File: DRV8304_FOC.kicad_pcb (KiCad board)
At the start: 4 copper layers, 49.5 x 30.2 mm, 63 parts, among them J2 Conn_01x03, J3 Conn_01x03, Q1 SIRA18ADP, Q2 SIRA18ADP, Q3 SIRA18ADP, Q4 SIRA18ADP, Q5 SIRA18ADP, Q6 SIRA18ADP, SW2 SW_Push, U1 TPS565208, U2 TPS259850RQPR, U3 DRV8304HRHAR, U4 STM32F412CEUx, U5 AS5055A, Y1 Crystal_GND23

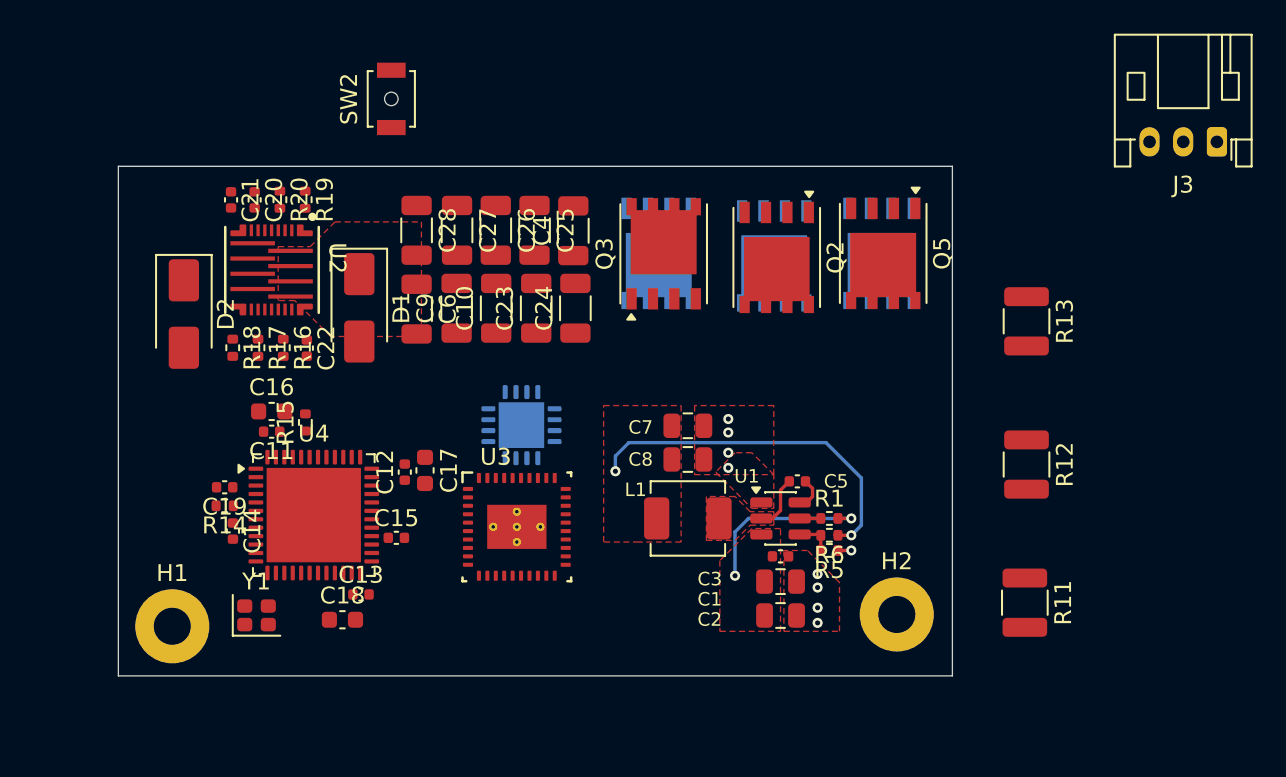
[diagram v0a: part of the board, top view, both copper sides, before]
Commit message: Modified encoder sch, modified layout
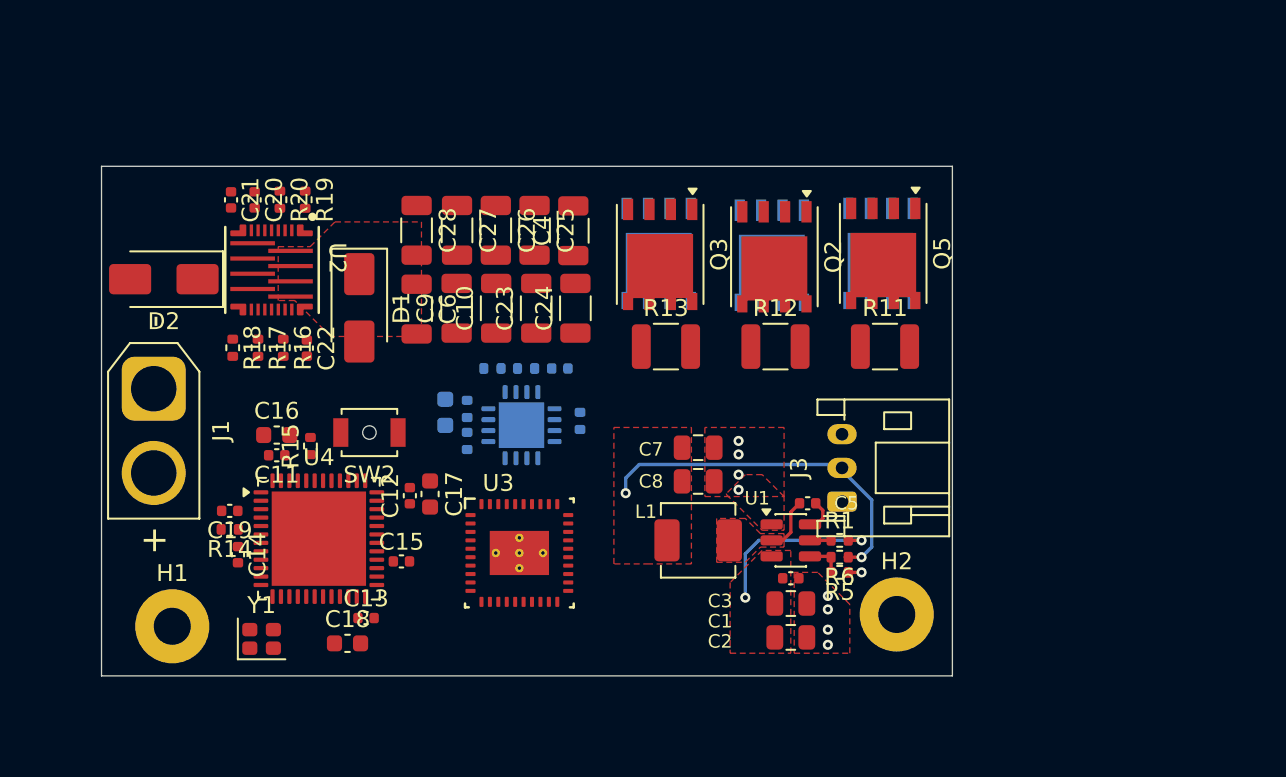
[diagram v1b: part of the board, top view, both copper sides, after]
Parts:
- added C29: 4.7uF, Capacitor_SMD:C_0603_1608Metric, B.Cu at (91.9, 70.4)
- added C30: 100nF, Capacitor_SMD:C_0402_1005Metric, B.Cu at (98.7, 67.8)
- added J1: Conn_01x02, Connector_AMASS:AMASS_XT30U-M_1x02_P5.0mm_Vertical, F.Cu at (74.6, 69.0)
- added R10: 22R, Resistor_SMD:R_0402_1005Metric, B.Cu at (93.2, 72.1)
- added R21: 10k, Resistor_SMD:R_0402_1005Metric, B.Cu at (96.7, 67.8)
- added R22: 22R, Resistor_SMD:R_0402_1005Metric, B.Cu at (99.9, 70.9)
- added R7: 15R, Resistor_SMD:R_0402_1005Metric, B.Cu at (93.2, 70.2)
- added R9: 22R, Resistor_SMD:R_0402_1005Metric, B.Cu at (94.7, 67.8)
- moved J3 30.8 mm to (115.5, 75.7), turned to 90 degrees
- moved R13 21.5 mm to (105.0, 66.5), turned to 0 degrees
- moved SW2 19.8 mm to (87.4, 71.6), turned to 180 degrees
- moved R11 17.3 mm to (118.0, 66.5), turned to 0 degrees
- moved R12 16.5 mm to (111.5, 66.5), turned to 0 degrees
- moved D2 2.39 mm to (75.2, 62.5), turned to 180 degrees
- moved U3 1.56 mm to (96.3, 78.7)
- moved C1 1.44 mm to (112.4, 81.7)
- moved C3 1.44 mm to (112.4, 80.2)
- moved C7 1.44 mm to (106.9, 72.5)
- moved C8 1.44 mm to (106.9, 74.5)
- moved L1 1.44 mm to (106.9, 78.0)
- moved R1 1.44 mm to (115.3, 78.0)
- moved R6 1.44 mm to (115.3, 79.0)
- moved U1 1.44 mm to (112.4, 78.0)
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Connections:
- U5 pad 1: unconnected-(U5-MOSI-Pad1) -> Net-(U5-MOSI)
- U5 pad 10: unconnected-(U5-~{EN_INT}-Pad10) -> GND
- U5 pad 11: unconnected-(U5-VDDp-Pad11) -> 3V3
- U5 pad 12: unconnected-(U5-VDD-Pad12) -> Net-(U5-VDD)
- U5 pad 13: unconnected-(U5-VSS-Pad13) -> GND
- U5 pad 14: unconnected-(U5-WM-Pad14) -> 3V3
- U5 pad 15: unconnected-(U5-~{INT}-Pad15) -> ~{INT}
- U5 pad 2: unconnected-(U5-MISO-Pad2) -> Net-(U5-MISO)
- U5 pad 3: unconnected-(U5-SCK-Pad3) -> Net-(U5-SCK)
- U5 pad 4: unconnected-(U5-~{SS}-Pad4) -> ~{SS}
- U5 pad 9: unconnected-(U5-TEST-Pad9) -> GND
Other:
- board size 49.5 x 30.2 mm -> 50.5 x 30.2 mm

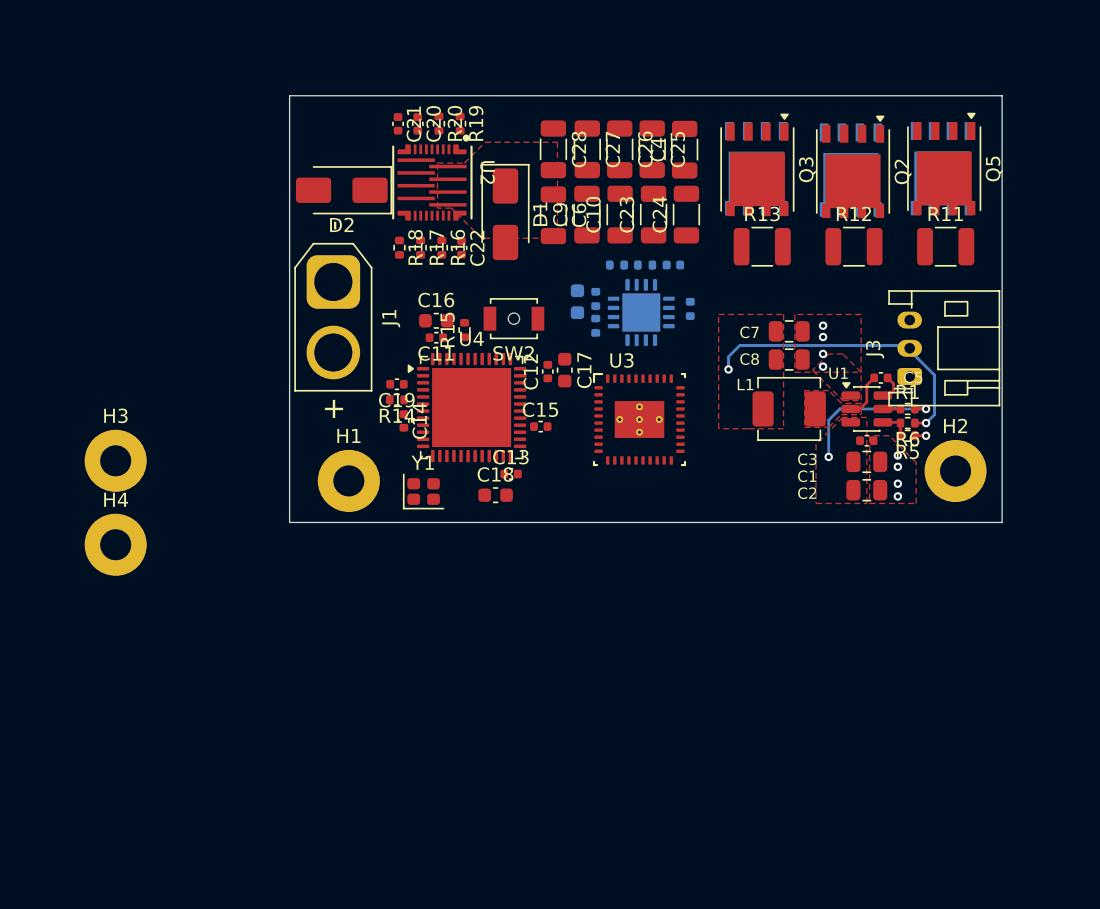
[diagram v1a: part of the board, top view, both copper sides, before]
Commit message: Replace buck converter with LDO
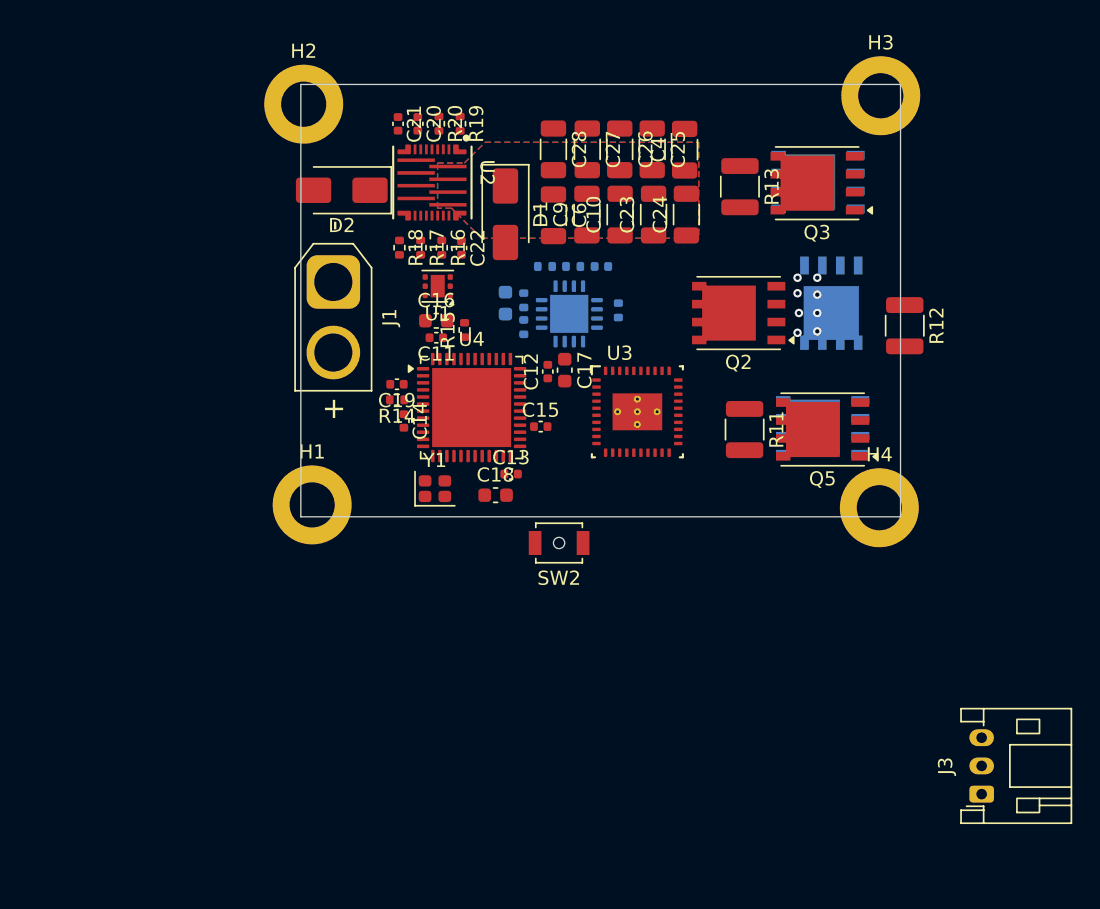
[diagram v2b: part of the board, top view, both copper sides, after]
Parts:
- removed C1, C2: 22uF, Capacitor_SMD:C_0805_2012Metric
- removed C3, C5: 0.1uF, Capacitor_SMD:C_0402_1005Metric
- removed C7, C8: 22u, Capacitor_SMD:C_0805_2012Metric
- removed L1: 3.3u, Inductor_SMD:L_APV_APH0420
- removed R1: 0, Resistor_SMD:R_0402_1005Metric
- removed R5: 10k, Resistor_SMD:R_0402_1005Metric
- removed R6: 13.7k, Resistor_SMD:R_0402_1005Metric
- H1, H2, H3, H4: footprint MountingHole:MountingHole_2.2mm_M2_Pad -> MountingHole:MountingHole_3.2mm_M3_DIN965_Pad
- U1: value TPS565208 -> TPS7A2633DRVR; footprint Package_TO_SOT_SMD:SOT-23-6 -> Package_SON:WSON-6-1EP_2x2mm_P0.65mm_EP1x1.6mm
- moved H3 60.1 mm to (113.4, 55.8)
- moved H4 54.2 mm to (113.3, 85.0)
- moved H2 53.0 mm to (72.5, 56.4)
- moved U1 31.6 mm to (82.0, 69.3), turned to 180 degrees
- moved J3 30.0 mm to (120.6, 105.3)
- moved Q5 20.4 mm to (109.3, 79.4), turned to 180 degrees
- moved Q6 20.2 mm to (109.3, 79.3), turned to 180 degrees
- moved R11 19.3 mm to (103.8, 79.4), turned to -90 degrees
- moved SW2 16.2 mm to (90.6, 87.5)
- moved Q2 12.9 mm to (103.3, 71.2), turned to 180 degrees
- moved Q1 9.53 mm to (109.9, 70.5)
- moved R12 6.66 mm to (115.1, 72.1), turned to -90 degrees
- moved C30 5.10 mm to (93.6, 67.9)
- moved R10 5.10 mm to (88.1, 72.2)
- moved R21 5.10 mm to (91.6, 67.9)
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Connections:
- U1 pad 1: GND -> unconnected-(U1-OUT-Pad1)
- U1 pad 2: Net-(U1-SW) -> unconnected-(U1-NC-Pad2)
- U1 pad 3: Vm -> unconnected-(U1-PG-Pad3)
- U1 pad 4: Net-(U1-VFB) -> unconnected-(U1-EN-Pad4)
- U1 pad 5: Net-(U1-EN) -> EPAD
- U1 pad 6: Net-(U1-VBST) -> unconnected-(U1-IN-Pad6)
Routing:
- net 3V3: track 21.3 -> 0.00 mm, vias 2 -> 0
- net Vm: track 10.8 -> 0.00 mm
- net Net-(U1-SW): track 3.27 -> 0.00 mm
- net Net-(U1-VFB): track 2.48 -> 0.00 mm
- net Net-(U1-VBST): track 2.38 -> 0.00 mm
- net Net-(U1-EN): track 1.44 -> 0.00 mm
- net GND: track 0.98 -> 0.00 mm, vias 9 -> 0
- net unconnected-(Q2-G-Pad2): vias 0 -> 4
- net unconnected-(Q1-G-Pad2): vias 0 -> 1
- net Vin: vias 2 -> 1
- net Net-(Q1-S): vias 0 -> 1
- net (no net): vias 0 -> 1
- added copper zone on B.Cu, net Vin
- added copper zone on In1.Cu, net Vin
- added copper zone on In2.Cu, net Vin
- removed copper zone on F.Cu, net 3V3
- removed copper zone on F.Cu, net GND
- removed copper zone on F.Cu, net Net-(U1-SW)
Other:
- board size 50.5 x 30.2 mm -> 42.5 x 30.6 mm

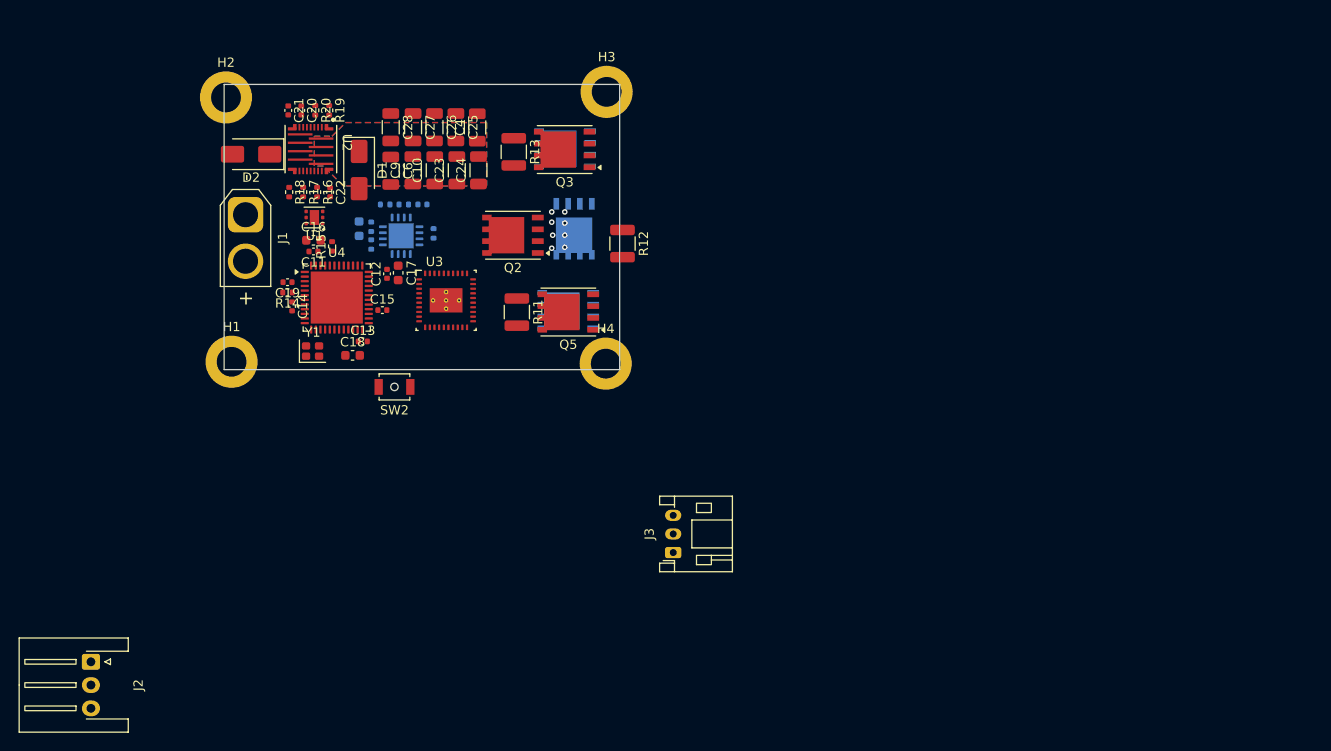
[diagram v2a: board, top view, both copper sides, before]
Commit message: Add buck back, changed board shape, replace cer cap with alu cap
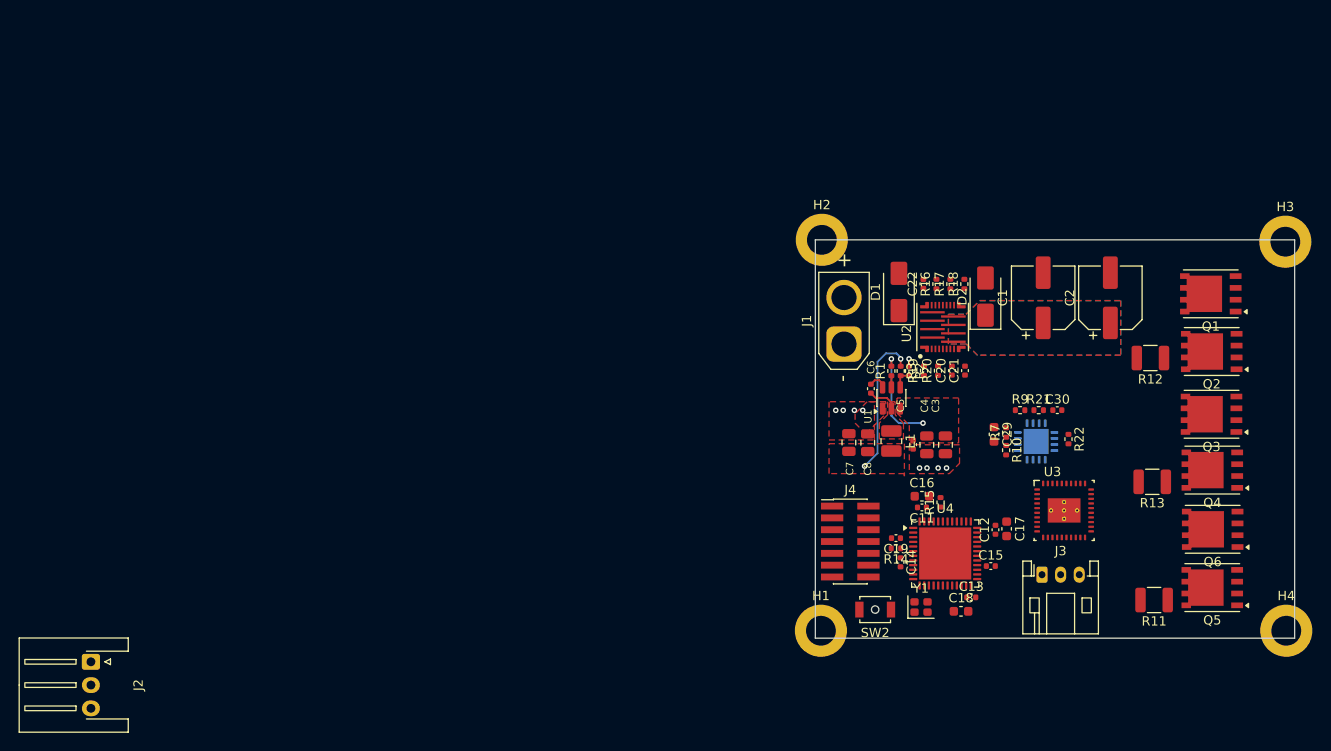
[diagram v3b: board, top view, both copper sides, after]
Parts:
- removed C10, C23, C24, C25, C26, C27, C28, C9: 22uF, Capacitor_SMD:C_1206_3216Metric
- added C1: C_Polarized, Capacitor_SMD:CP_Elec_6.3x7.7, F.Cu at (160.3, 77.9)
- added C2: C_Polarized, Capacitor_SMD:CP_Elec_6.3x7.7, F.Cu at (167.5, 77.9)
- added C3: 22u, Capacitor_SMD:C_0805_2012Metric, F.Cu at (149.8, 93.7)
- added C5: 0.1u, Capacitor_SMD:C_0402_1005Metric, F.Cu at (146.3, 93.7)
- added C7: 22u, Capacitor_SMD:C_0805_2012Metric, F.Cu at (139.4, 93.4)
- added C8: 22u, Capacitor_SMD:C_0805_2012Metric, F.Cu at (141.5, 93.5)
- added J4: Conn_02x07_Counter_Clockwise, Connector_PinHeader_1.27mm:PinHeader_2x07_P1.27mm_Vertical_SMD, F.Cu at (139.6, 104.1)
- added L1: 3.3u, Inductor_SMD:L_1008_2520Metric, F.Cu at (144.0, 93.3)
- added R1: 0, Resistor_SMD:R_0402_1005Metric, F.Cu at (144.0, 85.8)
- added R2: 10k, Resistor_SMD:R_0402_1005Metric, F.Cu at (145.9, 85.8)
- added R3: 13.7k, Resistor_SMD:R_0402_1005Metric, F.Cu at (145.0, 85.8)
- C29, C30, Q1, Q4, Q6, R10, R21, R22, R7, R9: moved to F.Cu
- C4: value 22uF -> 22u; footprint Capacitor_SMD:C_1206_3216Metric -> Capacitor_SMD:C_0805_2012Metric
- C6: value 22uF -> 0.1u; footprint Capacitor_SMD:C_1206_3216Metric -> Capacitor_SMD:C_0402_1005Metric
- U1: value TPS7A2633DRVR -> TPS565208; footprint Package_SON:WSON-6-1EP_2x2mm_P0.65mm_EP1x1.6mm -> Package_TO_SOT_SMD:SOT-23-6
- moved D2 80.4 mm to (154.1, 77.8), turned to 90 degrees
- moved H4 78.6 mm to (186.4, 113.7)
- moved C21 77.9 mm to (151.9, 85.7), turned to 90 degrees
- moved Q4 77.6 mm to (178.5, 96.4)
- moved R13 77.2 mm to (172.0, 97.7), turned to 180 degrees
- moved Q2 76.1 mm to (178.4, 83.7)
- moved C20 75.3 mm to (150.5, 85.7), turned to 90 degrees
- moved Q5 75.3 mm to (178.5, 109.0)
- moved R11 75.1 mm to (172.2, 110.4), turned to 180 degrees
- moved Q3 75.1 mm to (178.4, 90.4)
- moved H3 74.7 mm to (186.3, 71.9)
- moved R18 73.2 mm to (151.8, 76.4), turned to 90 degrees
- moved Q6 73.1 mm to (178.5, 102.8)
- moved R20 72.5 mm to (149.0, 85.7), turned to 90 degrees
- moved C30 71.7 mm to (161.8, 90.0), turned to 0 degrees
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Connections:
- C4 pad 1: Vm -> VIN
- C6 pad 1: unconnected-(C6-Pad1) -> Net-(U1-VBST)
- C6 pad 2: unconnected-(C6-Pad2) -> Net-(U1-SW)
- U1 pad 1: unconnected-(U1-OUT-Pad1) -> GND
- U1 pad 2: unconnected-(U1-NC-Pad2) -> Net-(U1-SW)
- U1 pad 3: unconnected-(U1-PG-Pad3) -> VIN
- U1 pad 4: unconnected-(U1-EN-Pad4) -> Net-(U1-VFB)
- U1 pad 5: EPAD -> Net-(U1-EN)
- U1 pad 6: unconnected-(U1-IN-Pad6) -> Net-(U1-VBST)
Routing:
- net 1V8: track 0.00 -> 16.0 mm, vias 0 -> 2
- net VIN: track 0.00 -> 10.8 mm, vias 0 -> 2
- net Net-(U1-SW): track 0.00 -> 3.27 mm
- net Net-(U1-VBST): track 0.00 -> 2.38 mm
- net Net-(U1-VFB): track 0.00 -> 2.21 mm
- net Net-(U1-EN): track 0.00 -> 1.44 mm
- net GND: track 0.00 -> 0.98 mm, vias 0 -> 9
- net unconnected-(Q2-G-Pad2): vias 4 -> 0
- net unconnected-(Q1-G-Pad2): vias 1 -> 0
- net Vin: vias 1 -> 0
- net Net-(Q1-S): vias 1 -> 0
- net (no net): vias 1 -> 0
- added copper zone on F.Cu, net 1V8
- added copper zone on F.Cu, net GND
- added copper zone on F.Cu, net Net-(U1-SW)
- added copper zone on F.Cu, net VIN
- added copper zone on B.Cu, net Vm
- added copper zone on F.Cu, net Vm
- added copper zone on In1.Cu, net Vm
- added copper zone on In2.Cu, net Vm
- removed copper zone on B.Cu, net Vin
- removed copper zone on F.Cu, net Vin
- removed copper zone on In1.Cu, net Vin
- removed copper zone on In2.Cu, net Vin
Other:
- board size 42.5 x 30.6 mm -> 51.5 x 42.8 mm
